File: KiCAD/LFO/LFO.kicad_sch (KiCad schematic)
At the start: 13 parts, among them J3 OUT, J4 OUT, J5 Conn_01x03, J6 Conn_01x03, SW1 SW_SPDT, U1 TL072

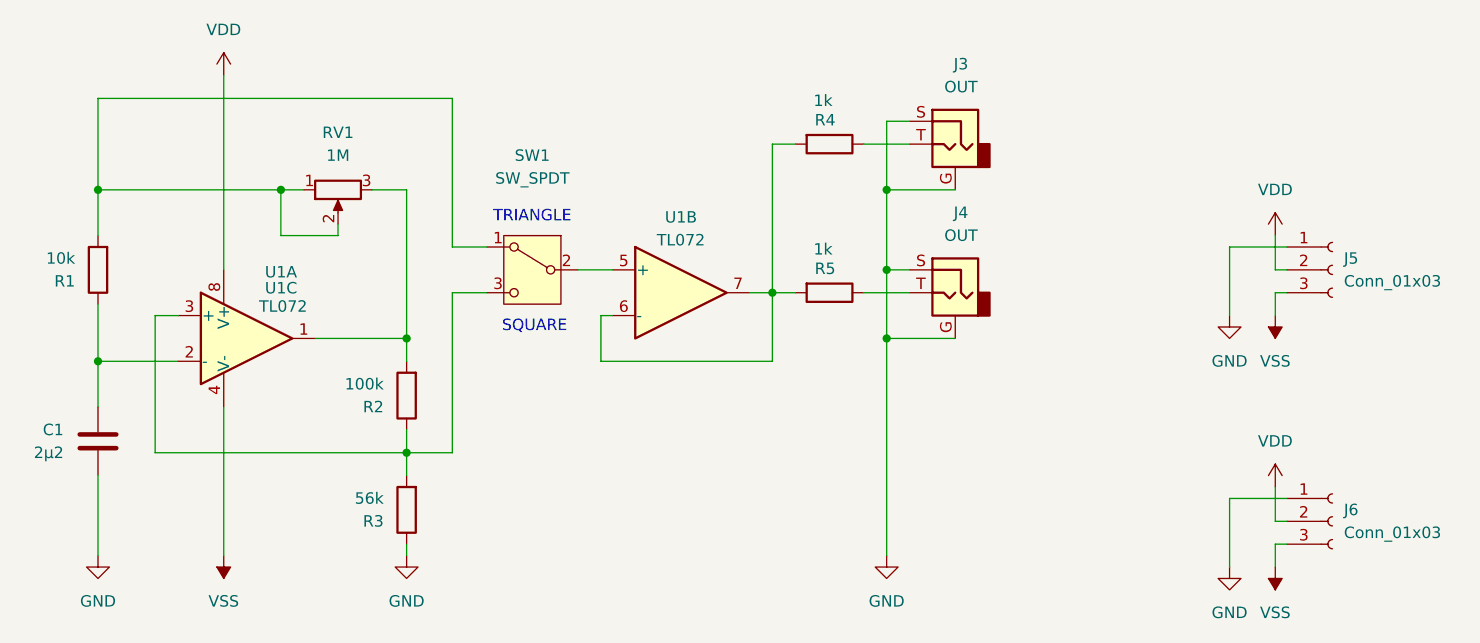
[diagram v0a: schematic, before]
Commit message: LFO PCB
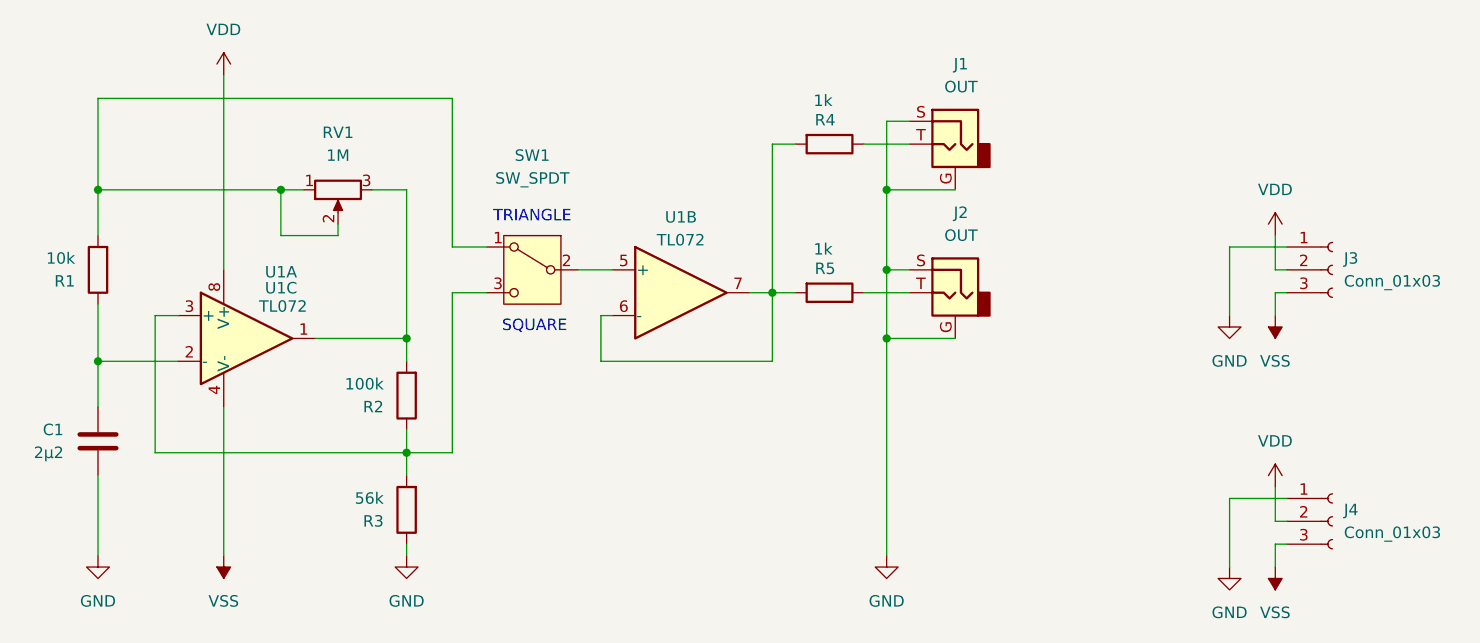
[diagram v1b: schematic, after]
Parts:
- SW1: footprint (none) -> HackSynth:Switch SPDT - MTS-102
- renumbered J3 to J1, J4 to J2, J5 to J3, J6 to J4
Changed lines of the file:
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@@
 			"AAAAAAAABQAAAAAAAAAAAAAAAAAAAAUAAAAAAAAAAAAAAAAAAAAFAAAAAAAAAAAAAAAAAAAABQAA"
 			"AAAAAAAAAAAAAAAAAAUAAAAAAAAAAAAAAAAAAAAFAAAAAAAAAAAAAAAAAAAABQAAAAAAAAAAAAAA"
-			"AAAAAAU="
+			"AAAAAAUAAAAAAAAAAAAAAAAAAAAAAAAAAAAAAAAAAAAAAAAAAAAAAAAAAAAAAAAAAAAAAAAAAAAA"
+			"AAAAAAAAAAAAAAAAAAAAAAAAAAAAAAAAAAAAAAAAAAAAAAAAAAAAAAAAAAAAAAAAAAAAAAAAAAAA"
+			"AAAAAAAAAAAAAAAAAAAAAAAAAAAAAAAAAAAAAAAAAAAAAAAAAAAAAAAAAAAAAAAAAAAAAAAAAAAA"
+			"AAAAAAAAAAAAAAAAAAAAAAAAAAAAAAAAAAAAAAAAAAAAAAAAAAAAAAAAAAAAAAAAAAAAAAAAAAAA"
+			"AAAAAAAAAAAAAAAAAAAAAAAAAAAAAAAAAAAAAAAAAAAAAAAAAAAAAAAAAAAAAAAAAAAAAAAAAAAA"
+			"AAAAAAAAAAAAAAAAAAAAAAAAAAAAAAAAAAAAAAAAAAAAAAAAAAAAAAAAAAAAAAAAAAAAAAAAAAAA"
+			"AAAAAAAAAAAAAAAAAAAAAAAAAAAAAAAAAAAAAAAAAAAAAAAAAAAAAAAAAAAAAAAAAAAAAAAAAAAA"
+			"AAAAAAAAAAAAAAAAAAAAAAAAAAAAAAAAAAAAAAAAAAAAAAAAAAAAAAAAAAAAAAAAAAAAAAAAAAAA"
+			"AAAAAAAAAAAAAAAAAAAAAAAAAAAAAAAAAAAAAAAAAAAAAAAAAAAAAAAAAAAAAAAAAAAAAAAAAAAA"
+			"AAAAAAAAAAAAAAAAAAAAAAAAAAAAAAAAAAAAAAAAAAAAAAAAAAAAAAAAAAAAAAAAAAAAAAAAAAAA"
+			"AAAAAAAAAAAAAAAAAAAAAAAAAAAAAAAAAAAAAAAAAAAAAAAAAAAAAAAAAAAAAAAAAAAAAAAAAAAA"
+			"AAAAAAAAAAAAAAAAAAAAAAAAAAAAAAAAAAAAAAAAAAAAAAAAAAAAAAAAAAAAAAAAAAAAAAAAAAAA"
+			"AAAAAAAAAAAAAAAAAAAAAAAAAAAAAAAAAAAAAAAAAAAAAAAAAAAAAAAAAAAAAAAAAAAAAAAAAAAA"
+			"AAAAAAAAAAAAAAAAAAAAAAAAAAAAAAAAAAAAAAAAAAAAAAAAAAAAAAAAAAAAAAAAAAAAAAAAAAAA"
+			"AAAAAAAAAAAAAAAAAAAAAAAAAAAAAAAAAAAAAAAAAAAAAAAAAAAAAAAAAAAAAAAAAAAAAAAAAAAA"
+			"AAAAAAAAAAAAAAAAAAAAAAAAAAAAAAAAAAAAAAAAAAAAAAAAAAAAAAAAAAAAAAAAAAAAAAAAAAAA"
+			"AAAAAAAAAAAAAAAAAAAAAAAAAAAAAAAAAAAAAAAAAAAAAAAAAAAAAAAAAAAAAAAAAAAAAAAAAAAA"
+			"AAAAAAAAAAAAAAAAAAAAAAAAAAAAAAAAAAAAAAAAAAAAAAAAAAAAAAAAAAAAAAAAAAAAAAAAAAAA"
+			"AAAAAA=="
 		)
 	)
@@
 			)
 		)
-		(property "Footprint" ""
+		(property "Footprint" "HackSynth:Switch SPDT - MTS-102"
 			(at 97.79 102.87 0)
 			(effects
@@
 		(dnp no)
 		(fields_autoplaced yes)
-		(property "Reference" "J6"
+		(property "Reference" "J4"
 			(at 187.96 129.5399 0)
 			(effects
@@
 			(project "LFO"
 				(path "/cf31493f-2592-4a10-a419-2df89491bd24"
-					(reference "J6")
+					(reference "J4")
 					(unit 1)
 				)
@@
 		(on_board yes)
 		(dnp no)
-		(property "Reference" "J3"
+		(property "Reference" "J1"
 			(at 145.415 80.01 0)
 			(effects
@@
 			(project "LFO"
 				(path "/cf31493f-2592-4a10-a419-2df89491bd24"
-					(reference "J3")
+					(reference "J1")
 					(unit 1)
 				)
@@
 		(dnp no)
 		(fields_autoplaced yes)
-		(property "Reference" "J5"
+		(property "Reference" "J3"
 			(at 187.96 101.5999 0)
 			(effects
@@
 			(project "LFO"
 				(path "/cf31493f-2592-4a10-a419-2df89491bd24"
-					(reference "J5")
+					(reference "J3")
 					(unit 1)
 				)
@@
 		(on_board yes)
 		(dnp no)
-		(property "Reference" "J4"
+		(property "Reference" "J2"
 			(at 145.415 96.52 0)
 			(effects
@@
 			(project "LFO"
 				(path "/cf31493f-2592-4a10-a419-2df89491bd24"
-					(reference "J4")
-					(unit 1)
-				)
+					(reference "J2")
+					(unit 1)
+				)

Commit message: Library updates
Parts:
- C1: footprint HackSynth:C_Disc_D5.0mm_W2.5mm_P5.00mm -> HackSynth:C_Radial_Tantal_D4.5mm_P5.00mm
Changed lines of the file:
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@@
+			"AAAAAAAAAAAAAAAAAAAAAAAAAAAAAAAAAAAAAAAAAAAAAAAAAAAAAAAAAAAAAAAAAAAAAAAAAAAA"
+			"AAAAAAAAAAAAAAAAAAAAAAAAAAAAAAAAAAAAAAAAAAAAAAAAAAAAAAAAAAAAAAAAAAAAAAAAAAAA"
+			"AAAAAAAAAAAAAAAAAAAAAAAAAAAAAAAAAAAAAAAAAAAAAAAAAAAAAAAAAAAAAAAAAAAAAAAAAAAA"
+			"AAAAAAAAAAAAAAAAAAAAAAAAAAAAAAAAAAAAAAAAAAAAAAAAAAAAAAAAAAAAAAAAAAAAAAAAAAAA"
+			"AAAAAAAAAAAAAAAAAAAAAAAAAAAAAAAAAAAAAAAAAAAAAAAAAAAAAAAAAAAAAAAAAAAAAAAAAAAA"
+			"AAAAAAAAAAAAAAAAAAAAAAAAAAAAAAAAAAAAAAAAAAAAAAAAAAAAAAAAAAAAAAAAAAAAAAAAAAAA"
+			"AAAAAAAAAAAAAAAAAAAAAAAAAAAAAAAAAAAAAAAAAAAAAAAAAAAAAAAAAAAAAAAAAAAAAAAAAAAA"
+			"AAAAAAAAAAAAAAAAAAAAAAAAAAAAAAAAAAAAAAAAAAAAAAAAAAAAAAAAAAAAAAAAAAAAAAAAAAAA"
+			"AAAAAAAAAAAAAAAAAAAAAAAAAAAAAAAAAAAAAAAAAAAAAAAAAAAAAAAAAAAAAAAAAAAAAAAAAAAA"
+			"AAAAAAAAAAAAAAAAAAAAAAAAAAAAAAAAAAAAAAAAAAAAAAAAAAAAAAAAAAAAAAAAAAAAAAAAAAAA"
+			"AAAAAAAAAAAAAAAAAAAAAAAAAAAAAAAAAAAAAAAAAAAAAAAAAAAAAAAAAAAAAAAAAAAAAAAAAAAA"
+			"AAAAAAAAAAAAAAAAAAAAAAAAAAAAAAAAAAAAAAAAAAAAAAAAAAAAAAAAAAAAAAAAAAAAAAAAAAAA"
+			"AAAAAAAAAAAAAAAAAAAAAAAAAAAAAAAAAAAAAAAAAAAAAAAAAAAAAAAAAAAAAAAAAAAAAAAAAAAA"
+			"AAAAAAAAAAAAAAAAAAAAAAAAAAAAAAAAAAAAAAAAAAAAAAAAAAAAAAAAAAAAAAAAAAAAAAAAAAAA"
+			"AAAAAAAAAAAAAAAAAAAAAAAAAAAAAAAAAAAAAAAAAAAAAAAAAAAAAAAAAAAAAAAAAAAAAAAAAAAA"
+			"AAAAAAAAAAAAAAAAAAAAAAAAAAAAAAAAAAAAAAAAAAAAAAAAAAAAAAAAAAAAAAAAAAAAAAAAAAAA"
+			"AAAAAAAAAAAAAAAAAAAAAAAAAAAAAAAAAAAAAAAAAAAAAAAAAAAAAAAAAAAAAAAAAAAAAAAAAAAA"
+			"AAAAAAAAAAAAAAAAAAAAAAAAAAAAAAAAAAAAAAAAAAAAAAAAAAAAAAAAAAAAAAAAAAAAAAAAAAAA"
 			"AAAAAAAAAAAAAAAAAAAAAAAAAAAAAAAAAAAAAAAAAAAAAAAAAAAAAAAAAAAAAAAAAAAAAAAAAAAA"
 			"AAAAAAAAAAAAAAAAAAAAAAAAAAAAAAAAAAAAAAAAAAAAAAAAAAAAAAAAAAAAAAAAAAAAAAAAAAAA"
@@
 			)
 		)
-		(property "Footprint" "HackSynth:C_Disc_D5.0mm_W2.5mm_P5.00mm"
+		(property "Footprint" "HackSynth:C_Radial_Tantal_D4.5mm_P5.00mm"
 			(at 48.5648 125.73 0)
 			(effects

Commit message: ASDR Schematic + LFO Gerbers
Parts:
- C1: footprint HackSynth:C_Radial_Tantal_D4.5mm_P5.00mm -> HackSynth:C_Ceramic_D4.5mm_P5.00mm
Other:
- moved on the sheet: J3, J4
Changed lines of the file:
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@@
 	(wire
 		(pts
-			(xy 180.34 99.06) (xy 180.34 102.87)
+			(xy 170.18 99.06) (xy 170.18 102.87)
 		)
 		(stroke
@@
 	(wire
 		(pts
-			(xy 181.61 105.41) (xy 180.34 105.41)
+			(xy 171.45 105.41) (xy 170.18 105.41)
 		)
 		(stroke
@@
 	(wire
 		(pts
-			(xy 180.34 127) (xy 180.34 130.81)
+			(xy 170.18 127) (xy 170.18 130.81)
 		)
 		(stroke
@@
 	(wire
 		(pts
-			(xy 175.26 100.33) (xy 175.26 107.95)
+			(xy 165.1 100.33) (xy 165.1 107.95)
 		)
 		(stroke
@@
 	(wire
 		(pts
-			(xy 180.34 130.81) (xy 181.61 130.81)
+			(xy 170.18 130.81) (xy 171.45 130.81)
 		)
 		(stroke
@@
 	(wire
 		(pts
-			(xy 180.34 133.35) (xy 180.34 135.89)
+			(xy 170.18 133.35) (xy 170.18 135.89)
 		)
 		(stroke
@@
 	(wire
 		(pts
-			(xy 181.61 128.27) (xy 175.26 128.27)
+			(xy 171.45 128.27) (xy 165.1 128.27)
 		)
 		(stroke
@@
 	(wire
 		(pts
-			(xy 175.26 128.27) (xy 175.26 135.89)
+			(xy 165.1 128.27) (xy 165.1 135.89)
 		)
 		(stroke
@@
 	(wire
 		(pts
-			(xy 181.61 133.35) (xy 180.34 133.35)
+			(xy 171.45 133.35) (xy 170.18 133.35)
 		)
 		(stroke
@@
 	(wire
 		(pts
-			(xy 180.34 102.87) (xy 181.61 102.87)
+			(xy 170.18 102.87) (xy 171.45 102.87)
 		)
 		(stroke
@@
 	(wire
 		(pts
-			(xy 180.34 105.41) (xy 180.34 107.95)
+			(xy 170.18 105.41) (xy 170.18 107.95)
 		)
 		(stroke
@@
 	(wire
 		(pts
-			(xy 181.61 100.33) (xy 175.26 100.33)
+			(xy 171.45 100.33) (xy 165.1 100.33)
 		)
 		(stroke
@@
 			"AAAAAAAAAAAAAAAAAAAAAAAAAAAAAAAAAAAAAAAAAAAAAAAAAAAAAAAAAAAAAAAAAAAAAAAAAAAA"
 			"AAAAAAAAAAAAAAAAAAAAAAAAAAAAAAAAAAAAAAAAAAAAAAAAAAAAAAAAAAAAAAAAAAAAAAAAAAAA"
-			"AAAAAA=="
+			"AAAAAP//////////////////////////////////////////////////////////////////////"
+			"////////////////////////////////////////////////////////////////////////////"
+			"////////////////////////////////////////////////////////////////////////////"
+			"////////////////////////////////////////////////////////////////////////////"
+			"////////////////////////////////////////////////////////////////////////////"
+			"////////////////////////////////////////////////////////////////////////////"
+			"////////////////////////////////////////////////////////////////////////////"
+			"////////////////////////////////////////////////////////////////////////////"
+			"////////////////////////////////////////////////////////////////////////////"
+			"////////////////////////////////////////////////////////////////////////////"
+			"////////////////////////////////////////////////////////////////////////////"
+			"////////////////////////////////////////////////////////////////////////////"
+			"////////////////////////////////////////////////////////////////////////////"
+			"////////////////////////////////////////////////////////////////////////////"
+			"////////////////////////////////////////////////////////////////////////////"
+			"////////////////////////////////////////////////////////////////////////////"
+			"////////////////////////////////////////////////////////////////////////////"
+			"////////////////////////////////////////////////////////////////////////////"
+			"/////w=="
 		)
 	)
@@
 	(symbol
 		(lib_id "power:VDD")
-		(at 180.34 127 0)
+		(at 170.18 127 0)
 		(unit 1)
 		(exclude_from_sim no)
@@
 		(fields_autoplaced yes)
 		(property "Reference" "#PWR017"
-			(at 180.34 130.81 0)
+			(at 170.18 130.81 0)
 			(effects
 				(font
@@
 		)
 		(property "Value" "VDD"
-			(at 180.34 121.92 0)
+			(at 170.18 121.92 0)
 			(effects
 				(font
@@
 		)
 		(property "Footprint" ""
-			(at 180.34 127 0)
+			(at 170.18 127 0)
 			(effects
 				(font
@@
 		)
 		(property "Datasheet" ""
-			(at 180.34 127 0)
+			(at 170.18 127 0)
 			(effects
 				(font
@@
 		)
 		(property "Description" "Power symbol creates a global label with name \"VDD\""
-			(at 180.34 127 0)
+			(at 170.18 127 0)
 			(effects
 				(font
@@
 	(symbol
 		(lib_id "Connector:Conn_01x03_Socket")
-		(at 186.69 130.81 0)
+		(at 176.53 130.81 0)
 		(unit 1)
 		(exclude_from_sim no)
@@
 		(fields_autoplaced yes)
 		(property "Reference" "J4"
-			(at 187.96 129.5399 0)
+			(at 177.8 129.5399 0)
 			(effects
 				(font
@@
 		)
 		(property "Value" "Conn_01x03"
-			(at 187.96 132.0799 0)
+			(at 177.8 132.0799 0)
 			(effects
 				(font
@@
 		)
 		(property "Footprint" "HackSynth:JST_PH_S3B-PH-K_1x03_P2.00mm_Horizontal"
-			(at 186.69 130.81 0)
+			(at 176.53 130.81 0)
 			(effects
 				(font
@@
 		)
 		(property "Datasheet" "~"
-			(at 186.69 130.81 0)
+			(at 176.53 130.81 0)
 			(effects
 				(font
@@
 		)
 		(property "Description" "Generic connector, single row, 01x03, script generated"
-			(at 186.69 130.81 0)
+			(at 176.53 130.81 0)
 			(effects
 				(font
@@
 			)
 		)
-		(property "Footprint" "HackSynth:C_Radial_Tantal_D4.5mm_P5.00mm"
+		(property "Footprint" "HackSynth:C_Ceramic_D4.5mm_P5.00mm"
 			(at 48.5648 125.73 0)
 			(effects
@@
 	(symbol
 		(lib_id "Connector:Conn_01x03_Socket")
-		(at 186.69 102.87 0)
+		(at 176.53 102.87 0)
 		(unit 1)
 		(exclude_from_sim no)
@@
 		(fields_autoplaced yes)
 		(property "Reference" "J3"
-			(at 187.96 101.5999 0)
+			(at 177.8 101.5999 0)
 			(effects
 				(font
@@
 		)
 		(property "Value" "Conn_01x03"
-			(at 187.96 104.1399 0)
+			(at 177.8 104.1399 0)
 			(effects
 				(font
@@
 		)
 		(property "Footprint" "HackSynth:JST_PH_S3B-PH-K_1x03_P2.00mm_Horizontal"
-			(at 186.69 102.87 0)
+			(at 176.53 102.87 0)
 			(effects
 				(font
@@
 		)
 		(property "Datasheet" "~"
-			(at 186.69 102.87 0)
+			(at 176.53 102.87 0)
 			(effects
 				(font
@@
 		)
 		(property "Description" "Generic connector, single row, 01x03, script generated"
-			(at 186.69 102.87 0)
+			(at 176.53 102.87 0)
 			(effects
 				(font
@@
 	(symbol
 		(lib_id "power:VSS")
-		(at 180.34 135.89 180)
+		(at 170.18 135.89 180)
 		(unit 1)
 		(exclude_from_sim no)
@@
 		(fields_autoplaced yes)
 		(property "Reference" "#PWR018"
-			(at 180.34 132.08 0)
+			(at 170.18 132.08 0)
 			(effects
 				(font
@@
 		)
 		(property "Value" "VSS"
-			(at 180.34 140.97 0)
+			(at 170.18 140.97 0)
 			(effects
 				(font
@@
 		)
 		(property "Footprint" ""
-			(at 180.34 135.89 0)
+			(at 170.18 135.89 0)
 			(effects
 				(font
@@
 		)
 		(property "Datasheet" ""
-			(at 180.34 135.89 0)
+			(at 170.18 135.89 0)
 			(effects
 				(font
@@
 		)
 		(property "Description" "Power symbol creates a global label with name \"VSS\""
-			(at 180.34 135.89 0)
+			(at 170.18 135.89 0)
 			(effects
 				(font
@@
 	(symbol
 		(lib_id "power:GND")
-		(at 175.26 107.95 0)
+		(at 165.1 107.95 0)
 		(unit 1)
 		(exclude_from_sim no)
@@
 		(dnp no)
 		(property "Reference" "#PWR013"
-			(at 175.26 114.3 0)
+			(at 165.1 114.3 0)
 			(effects
 				(font
@@
 		)
 		(property "Value" "GND"
-			(at 175.26 113.03 0)
+			(at 165.1 113.03 0)
 			(effects
 				(font
@@
 		)
 		(property "Footprint" ""
-			(at 175.26 107.95 0)
+			(at 165.1 107.95 0)
 			(effects
 				(font
@@
 		)
 		(property "Datasheet" ""
-			(at 175.26 107.95 0)
+			(at 165.1 107.95 0)
 			(effects
 				(font
@@
 		)
 		(property "Description" "Power symbol creates a global label with name \"GND\" , ground"
-			(at 175.26 107.95 0)
+			(at 165.1 107.95 0)
 			(effects
 				(font
@@
 	(symbol
 		(lib_id "power:VDD")
-		(at 180.34 99.06 0)
+		(at 170.18 99.06 0)
 		(unit 1)
 		(exclude_from_sim no)
@@
 		(fields_autoplaced yes)
 		(property "Reference" "#PWR014"
-			(at 180.34 102.87 0)
+			(at 170.18 102.87 0)
 			(effects
 				(font
@@
 		)
 		(property "Value" "VDD"
-			(at 180.34 93.98 0)
+			(at 170.18 93.98 0)
 			(effects
 				(font
@@
 		)
 		(property "Footprint" ""
-			(at 180.34 99.06 0)
+			(at 170.18 99.06 0)
 			(effects
 				(font
@@
 		)
 		(property "Datasheet" ""
-			(at 180.34 99.06 0)
+			(at 170.18 99.06 0)
 			(effects
 				(font
@@
 		)
 		(property "Description" "Power symbol creates a global label with name \"VDD\""
-			(at 180.34 99.06 0)
+			(at 170.18 99.06 0)
 			(effects
 				(font
@@
 	(symbol
 		(lib_id "power:VSS")
-		(at 180.34 107.95 180)
+		(at 170.18 107.95 180)
 		(unit 1)
 		(exclude_from_sim no)
@@
 		(fields_autoplaced yes)
 		(property "Reference" "#PWR015"
-			(at 180.34 104.14 0)
+			(at 170.18 104.14 0)
 			(effects
 				(font
@@
 		)
 		(property "Value" "VSS"
-			(at 180.34 113.03 0)
+			(at 170.18 113.03 0)
 			(effects
 				(font
@@
 		)
 		(property "Footprint" ""
-			(at 180.34 107.95 0)
+			(at 170.18 107.95 0)
 			(effects
 				(font
@@
 		)
 		(property "Datasheet" ""
-			(at 180.34 107.95 0)
+			(at 170.18 107.95 0)
 			(effects
 				(font
@@
 		)
 		(property "Description" "Power symbol creates a global label with name \"VSS\""
-			(at 180.34 107.95 0)
+			(at 170.18 107.95 0)
 			(effects
 				(font
@@
 	(symbol
 		(lib_id "power:GND")
-		(at 175.26 135.89 0)
+		(at 165.1 135.89 0)
 		(unit 1)
 		(exclude_from_sim no)
@@
 		(dnp no)
 		(property "Reference" "#PWR016"
-			(at 175.26 142.24 0)
+			(at 165.1 142.24 0)
 			(effects
 				(font
@@
 		)
 		(property "Value" "GND"
-			(at 175.26 140.97 0)
+			(at 165.1 140.97 0)
 			(effects
 				(font
@@
 		)
 		(property "Footprint" ""
-			(at 175.26 135.89 0)
+			(at 165.1 135.89 0)
 			(effects
 				(font
@@
 		)
 		(property "Datasheet" ""
-			(at 175.26 135.89 0)
+			(at 165.1 135.89 0)
 			(effects
 				(font
@@
 		)
 		(property "Description" "Power symbol creates a global label with name \"GND\" , ground"
-			(at 175.26 135.89 0)
+			(at 165.1 135.89 0)
 			(effects
 				(font

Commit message: Delay PCB
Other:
- title: (none) -> HackSynth LFO
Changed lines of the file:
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@@
 	(generator_version "9.0")
 	(paper "A4")
+	(title_block
+		(title "HackSynth LFO")
+		(date "2025-06-21")
+		(rev "1-0")
+	)
 	(text "SQUARE"
 		(exclude_from_sim no)

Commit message: Backup Cleanup
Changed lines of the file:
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@@
 		(dnp no)
 		(property "Reference" "R1"
-			(at 46.99 104.1401 0)
+			(at 47.498 101.854 0)
 			(effects
 				(font
@@
 		)
 		(property "Value" "10k"
-			(at 46.99 101.6001 0)
+			(at 47.498 103.8861 0)
 			(effects
 				(font
@@
 		(dnp no)
 		(property "Reference" "R2"
-			(at 81.28 118.1101 0)
+			(at 81.534 117.856 0)
 			(effects
 				(font
@@
 		)
 		(property "Value" "100k"
-			(at 81.28 115.5701 0)
+			(at 81.534 115.8239 0)
 			(effects
 				(font
@@
 		(dnp no)
 		(property "Reference" "R3"
-			(at 81.28 130.8101 0)
+			(at 81.28 128.524 0)
 			(effects
 				(font
@@
 		)
 		(property "Value" "56k"
-			(at 81.28 128.2701 0)
+			(at 81.28 130.3021 0)
 			(effects
 				(font
@@
 		(dnp no)
 		(property "Reference" "R4"
-			(at 129.1589 86.233 90)
-			(effects
-				(font
-					(size 1.27 1.27)
-				)
-				(justify left)
+			(at 130.81 86.614 90)
+			(effects
+				(font
+					(size 1.27 1.27)
+				)
 			)
 		)
 		(property "Value" "1k"
-			(at 129.032 84.074 90)
-			(effects
-				(font
-					(size 1.27 1.27)
-				)
-				(justify left)
+			(at 130.81 88.9 90)
+			(effects
+				(font
+					(size 1.27 1.27)
+				)
 			)
 		)
@@
 		(dnp no)
 		(property "Reference" "R5"
-			(at 129.1589 102.743 90)
-			(effects
-				(font
-					(size 1.27 1.27)
-				)
-				(justify left)
+			(at 130.81 103.124 90)
+			(effects
+				(font
+					(size 1.27 1.27)
+				)
 			)
 		)
 		(property "Value" "1k"
-			(at 129.032 100.584 90)
-			(effects
-				(font
-					(size 1.27 1.27)
-				)
-				(justify left)
-			)
-		)
+			(at 130.81 105.41 90)
+			(effects
+				(font
+					(size 1.27 1.27)
+				)
+			)
+		)
